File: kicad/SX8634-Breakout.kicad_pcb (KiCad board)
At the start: 4 copper layers, 42.7 x 32.5 mm, 8 parts, among them J1 Conn_01x12_Male, J2 Conn_01x06, J3 Conn_01x08, P1 CONN_01X01, U1 SX8634

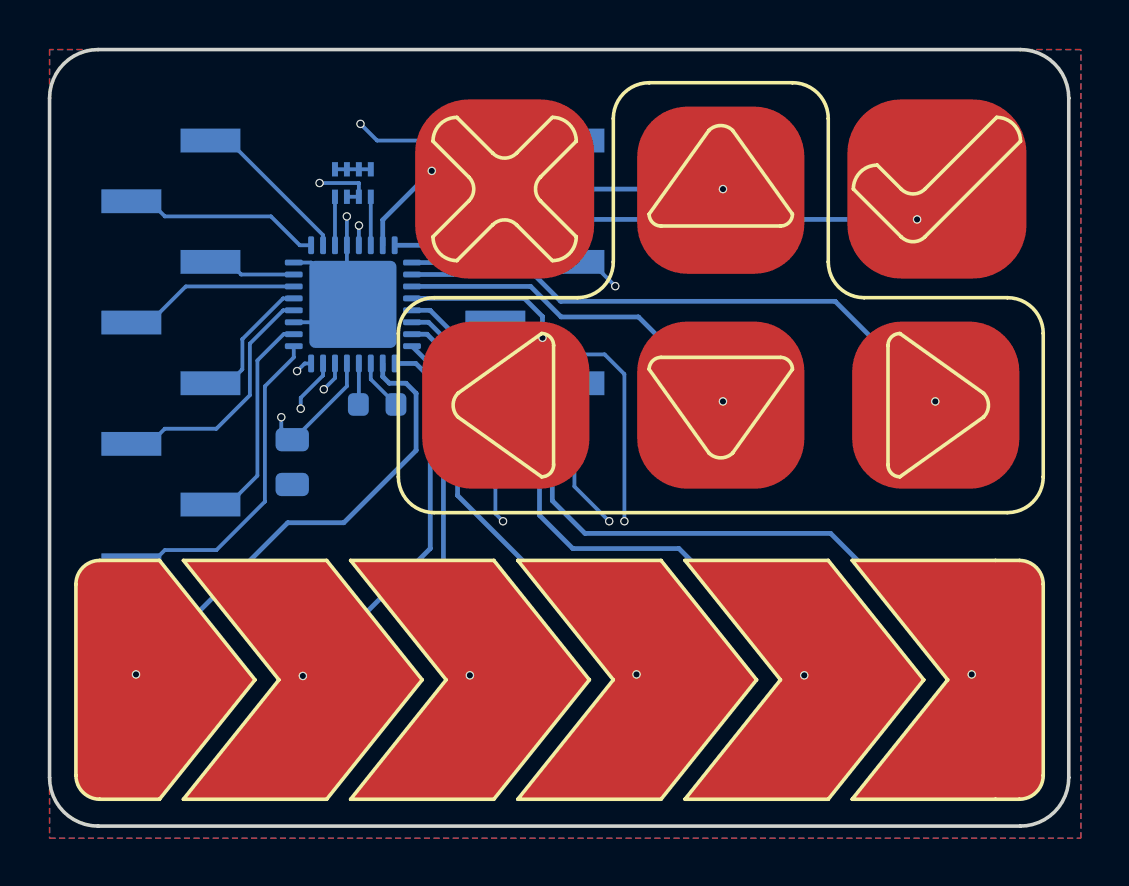
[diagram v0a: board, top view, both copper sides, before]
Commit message: Changing design for the sake of a cap array going obsolete.
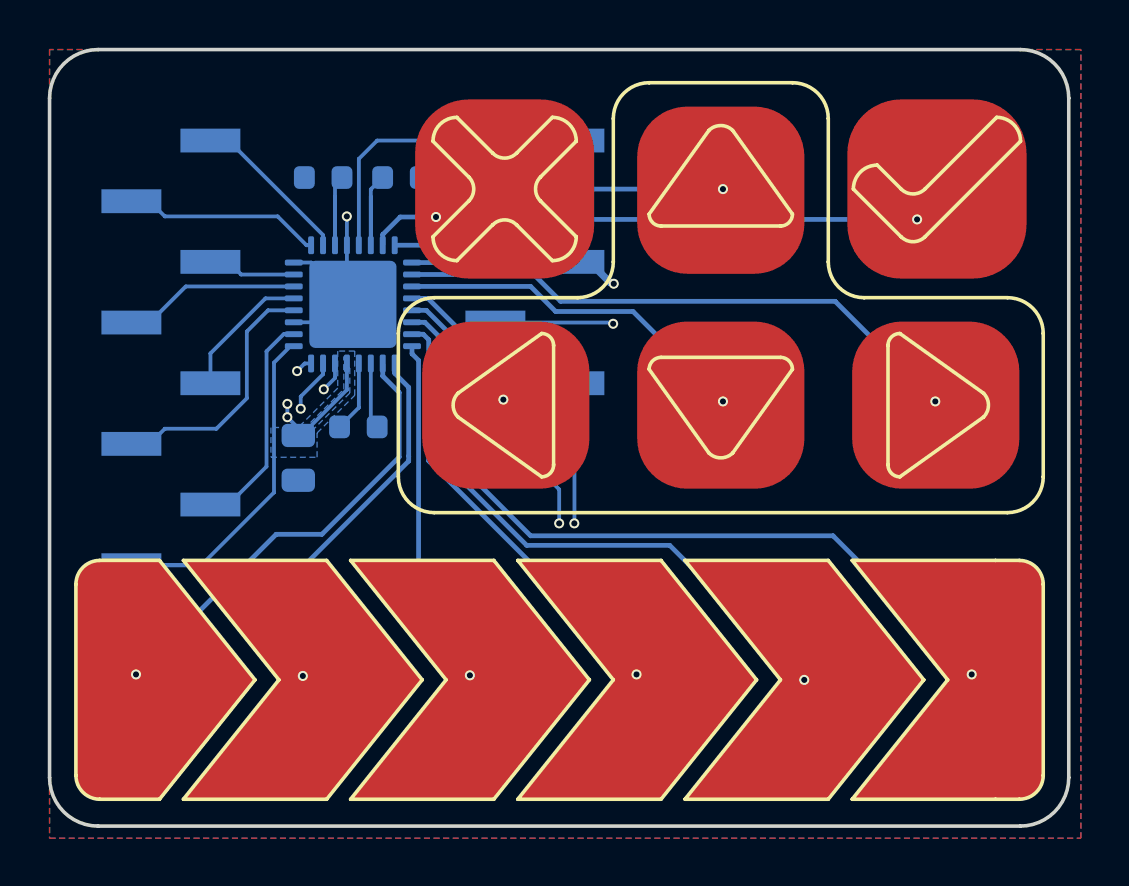
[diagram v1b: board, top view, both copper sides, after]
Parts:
- removed CARY1: 100nF, CapArray_CKCL44
- added C3: 100nF, Capacitor_SMD:C_0603_1608Metric, B.Cu at (63.0, 38.4)
- added C4: 100nF, Capacitor_SMD:C_0603_1608Metric, B.Cu at (59.7, 38.4)
- C2: value 1uF -> 100uF
- P1: footprint woose-tracker:ManuvrLogo -> kicad:ManuvrLogo
- moved C1 1.23 mm to (61.2, 48.8)
- moved C2 0.31 mm to (58.7, 50.1)
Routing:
- net /VCC: track 33.2 -> 9.95 mm
- net /~Touch_IRQ: track 30.2 -> 21.0 mm
- net /I2C_SCL: track 16.1 -> 21.3 mm
- net /cap10: track 16.5 -> 21.7 mm
- net /cap5: track 9.94 -> 6.49 mm
- net Net-(C3-Pad2): track 2.03 -> 5.07 mm
- net /GPIO0: track 13.7 -> 16.7 mm
- net Net-(C4-Pad2): track 2.03 -> 4.98 mm
- net GND: track 11.3 -> 9.77 mm
- net /~Touch_Reset: track 14.4 -> 13.0 mm, vias 2 -> 0
- net /cap6: track 31.5 -> 32.8 mm
- net Net-(C1-Pad1): track 1.72 -> 2.99 mm
- net /cap11: track 20.3 -> 19.0 mm
- net /cap0: track 7.32 -> 6.34 mm
- net /cap7: track 24.6 -> 25.6 mm
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- added copper zone on B.Cu, net /VCC
- added copper zone on In2.Cu, net /VCC
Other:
- net class Default: via_dia 0.354 -> 0.42
- net class SENSE_TRACES: via_dia 0.354 -> 0.42
